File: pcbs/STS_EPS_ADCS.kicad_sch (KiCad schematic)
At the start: 22 parts, among them U10 MAX11632EEGT, U5 MAX11632EEGT, U6 MAX11632EEGT, U7 MAX11632EEGT, U8 MAX11632EEGT, U9 MAX11632EEGT

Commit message: Worked on STS1_EPS_1 and STS1_EPS_2.
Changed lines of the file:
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@@
-    (effects (font (size 1.27 1.27)) (justify right bottom))
-  )
-  (label "BATT_I" (at 48.26 129.54 180)
     (effects (font (size 1.27 1.27)) (justify right bottom))
   )
@@
     (effects (font (size 1.27 1.27)) (justify right bottom))
   )
-  (label "CENTER" (at 48.26 127 180)
-    (effects (font (size 1.27 1.27)) (justify right bottom))
-  )
   (label "Panel_Y-_5" (at 48.26 137.16 180)
     (effects (font (size 1.27 1.27)) (justify right bottom))
@@
     (effects (font (size 1.27 1.27)) (justify left bottom))
   )
-  (label "BATT_TEMP" (at 48.26 132.08 180)
-    (effects (font (size 1.27 1.27)) (justify right bottom))
-  )
   (label "Panel_Z-_5" (at 111.76 57.15 180)
     (effects (font (size 1.27 1.27)) (justify right bottom))
@@
     (effects (font (size 1.27 1.27)) (justify right))
   )
+  (hierarchical_label "CENTER" (shape input) (at 48.26 127 180)
+    (effects (font (size 1.27 1.27)) (justify right))
+  )
   (hierarchical_label "COBC_SPI_[1..6]" (shape input) (at 29.21 19.05 180)
     (effects (font (size 1.27 1.27)) (justify right))
@@
     (effects (font (size 1.27 1.27)) (justify right))
   )
+  (hierarchical_label "BATT_TEMP" (shape input) (at 48.26 132.08 180)
+    (effects (font (size 1.27 1.27)) (justify right))
+  )
+  (hierarchical_label "BATT_I" (shape input) (at 48.26 129.54 180)
+    (effects (font (size 1.27 1.27)) (justify right))
+  )

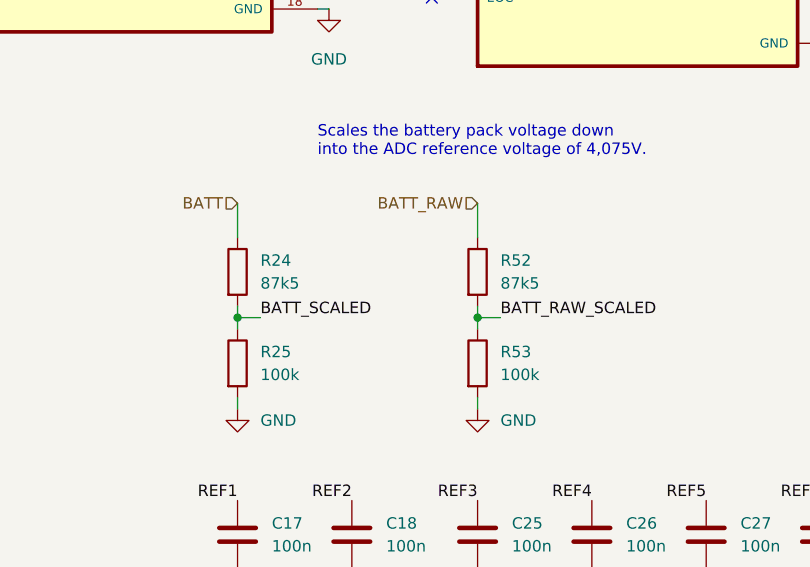
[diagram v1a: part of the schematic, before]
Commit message: Added part numbers to CSBI and inter EPS connectors. Also added some missing 3d files.
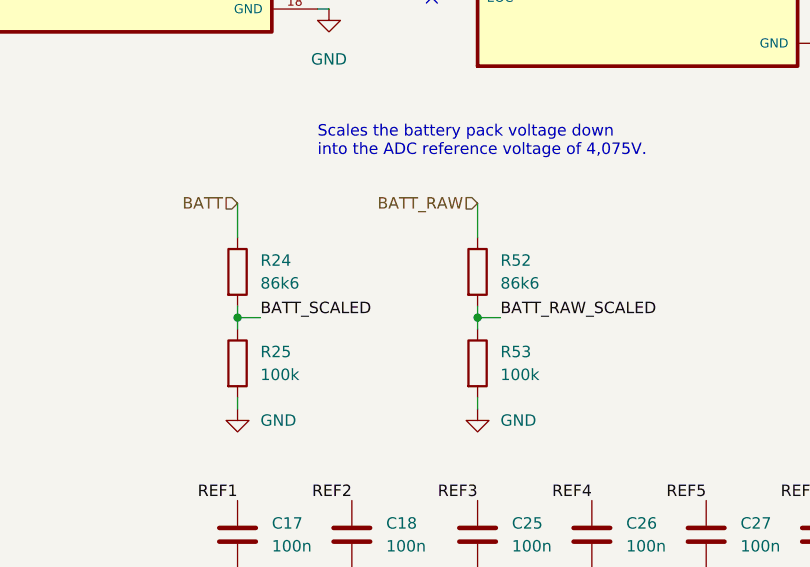
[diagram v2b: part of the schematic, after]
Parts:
- R24, R52: value 87k5 -> 86k6
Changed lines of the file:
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@@
       (effects (font (size 1.27 1.27)) (justify left))
     )
-    (property "Value" "87k5" (id 1) (at 210.82 125.7299 0)
+    (property "Value" "86k6" (id 1) (at 210.82 125.7299 0)
       (effects (font (size 1.27 1.27)) (justify left))
     )
@@
       (effects (font (size 1.27 1.27)) (justify left))
     )
-    (property "Value" "87k5" (id 1) (at 237.49 125.7299 0)
-      (effects (font (size 1.27 1.27)) (justify left))
-    )
+    (property "Value" "86k6" (id 1) (at 237.49 125.7299 0)
+      (effects (font (size 1.27 1.27)) (justify left))
+    )

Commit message: Fixed some warnings and errors.
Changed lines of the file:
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@@
 		)
 		(property "Value" "GND"
-			(at 210.82 140.9699 0)
+			(at 208.28 144.78 0)
 			(effects
 				(font
 					(size 1.27 1.27)
 				)
-				(justify left)
 			)
 		)
@@
 			)
 		)
-		(property "Description" ""
+		(property "Description" "Power symbol creates a global label with name \"GND\" , ground"
 			(at 208.28 139.7 0)
 			(effects
@@
 			)
 		)
-		(property "Description" ""
+		(property "Description" "Power symbol creates a global label with name \"GND\" , ground"
 			(at 247.65 157.48 0)
 			(effects
@@
 			)
 		)
-		(property "Description" ""
+		(property "Description" "Power symbol creates a global label with name \"GND\" , ground"
 			(at 109.22 158.75 0)
 			(effects
@@
 			)
 		)
-		(property "Description" ""
+		(property "Description" "Power symbol creates a global label with name \"GND\" , ground"
 			(at 283.21 30.48 0)
 			(effects
@@
 			)
 		)
-		(property "Description" ""
+		(property "Description" "Power symbol creates a global label with name \"GND\" , ground"
 			(at 96.52 182.88 0)
 			(effects
@@
 			)
 		)
-		(property "Description" ""
+		(property "Description" "Power symbol creates a global label with name \"GND\" , ground"
 			(at 160.02 186.69 0)
 			(effects
@@
 			)
 		)
-		(property "Description" ""
+		(property "Description" "Power symbol creates a global label with name \"GND\" , ground"
 			(at 166.37 26.67 0)
 			(effects
@@
 			)
 		)
-		(property "Description" ""
+		(property "Description" "Power symbol creates a global label with name \"GND\" , ground"
 			(at 273.05 157.48 0)
 			(effects
@@
 			)
 		)
-		(property "Description" ""
+		(property "Description" "Power symbol creates a global label with name \"GND\" , ground"
 			(at 171.45 34.29 0)
 			(effects
@@
 		)
 		(property "Value" "GND"
-			(at 237.49 140.9699 0)
+			(at 234.95 144.78 0)
 			(effects
 				(font
 					(size 1.27 1.27)
 				)
-				(justify left)
 			)
 		)
@@
 			)
 		)
-		(property "Description" ""
+		(property "Description" "Power symbol creates a global label with name \"GND\" , ground"
 			(at 234.95 139.7 0)
 			(effects
@@
 			)
 		)
-		(property "Description" ""
+		(property "Description" "Power symbol creates a global label with name \"GND\" , ground"
 			(at 226.06 26.67 0)
 			(effects
@@
 			)
 		)
-		(property "Description" ""
+		(property "Description" "Power symbol creates a global label with name \"GND\" , ground"
 			(at 96.52 95.25 0)
 			(effects
@@
 			)
 		)
-		(property "Description" ""
+		(property "Description" "Power symbol creates a global label with name \"GND\" , ground"
 			(at 260.35 157.48 0)
 			(effects
@@
 			)
 		)
-		(property "Description" ""
+		(property "Description" "Power symbol creates a global label with name \"GND\" , ground"
 			(at 220.98 157.48 0)
 			(effects
@@
 			)
 		)
-		(property "Description" ""
+		(property "Description" "Power symbol creates a global label with name \"GND\" , ground"
 			(at 208.28 157.48 0)
 			(effects
@@
 			)
 		)
-		(property "Description" ""
+		(property "Description" "Power symbol creates a global label with name \"GND\" , ground"
 			(at 111.76 125.73 0)
 			(effects
@@
 			)
 		)
-		(property "Description" ""
+		(property "Description" "Power symbol creates a global label with name \"GND\" , ground"
 			(at 170.18 67.31 0)
 			(effects
@@
 			)
 		)
-		(property "Description" ""
+		(property "Description" "Power symbol creates a global label with name \"GND\" , ground"
 			(at 48.26 154.94 0)
 			(effects
@@
 			)
 		)
-		(property "Description" ""
+		(property "Description" "Power symbol creates a global label with name \"GND\" , ground"
 			(at 279.4 99.06 0)
 			(effects
@@
 			)
 		)
-		(property "Description" ""
+		(property "Description" "Power symbol creates a global label with name \"GND\" , ground"
 			(at 166.37 118.11 0)
 			(effects
@@
 			)
 		)
-		(property "Description" ""
+		(property "Description" "Power symbol creates a global label with name \"GND\" , ground"
 			(at 102.87 114.3 0)
 			(effects
@@
 			)
 		)
-		(property "Description" ""
+		(property "Description" "Power symbol creates a global label with name \"GND\" , ground"
 			(at 160.02 95.25 0)
 			(effects
@@
 			)
 		)
-		(property "Description" ""
+		(property "Description" "Power symbol creates a global label with name \"GND\" , ground"
 			(at 101.6 26.67 0)
 			(effects
@@
 		)
 		(property "Value" "GND"
-			(at 218.44 100.838 0)
+			(at 218.44 100.33 0)
 			(effects
 				(font
@@
 			)
 		)
-		(property "Description" ""
+		(property "Description" "Power symbol creates a global label with name \"GND\" , ground"
 			(at 218.44 95.25 0)
 			(effects
@@
 			)
 		)
-		(property "Description" ""
+		(property "Description" "Power symbol creates a global label with name \"GND\" , ground"
 			(at 111.76 67.31 0)
 			(effects
@@
 			)
 		)
-		(property "Description" ""
+		(property "Description" "Power symbol creates a global label with name \"GND\" , ground"
 			(at 234.95 157.48 0)
 			(effects

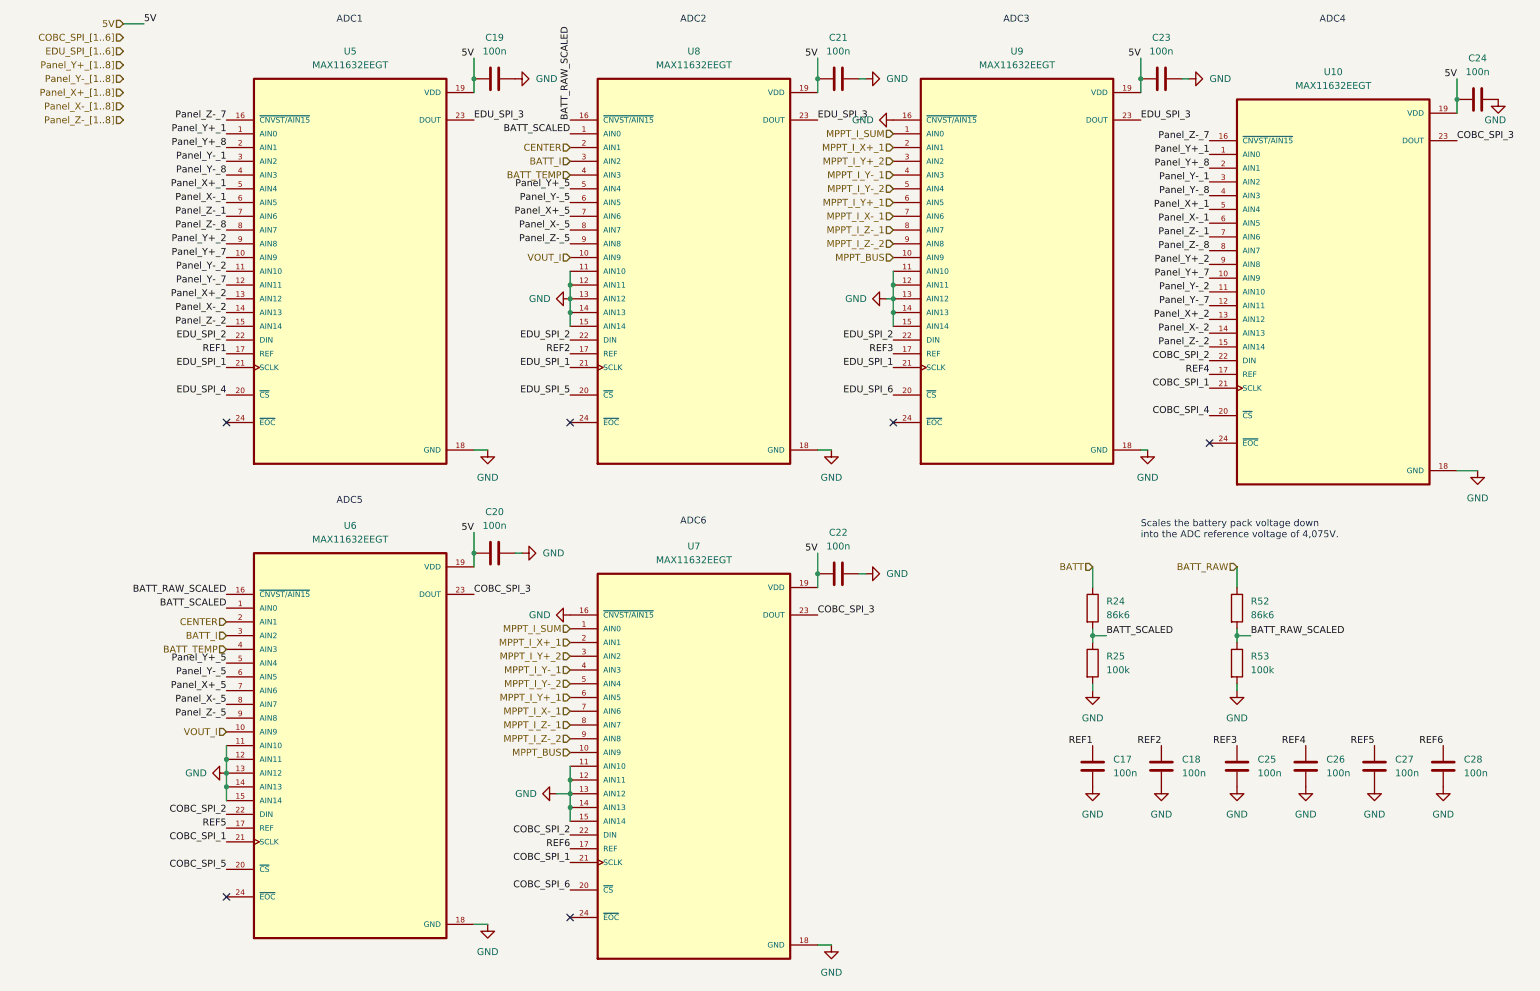
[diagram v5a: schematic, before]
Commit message: Fixed warnings and errors.
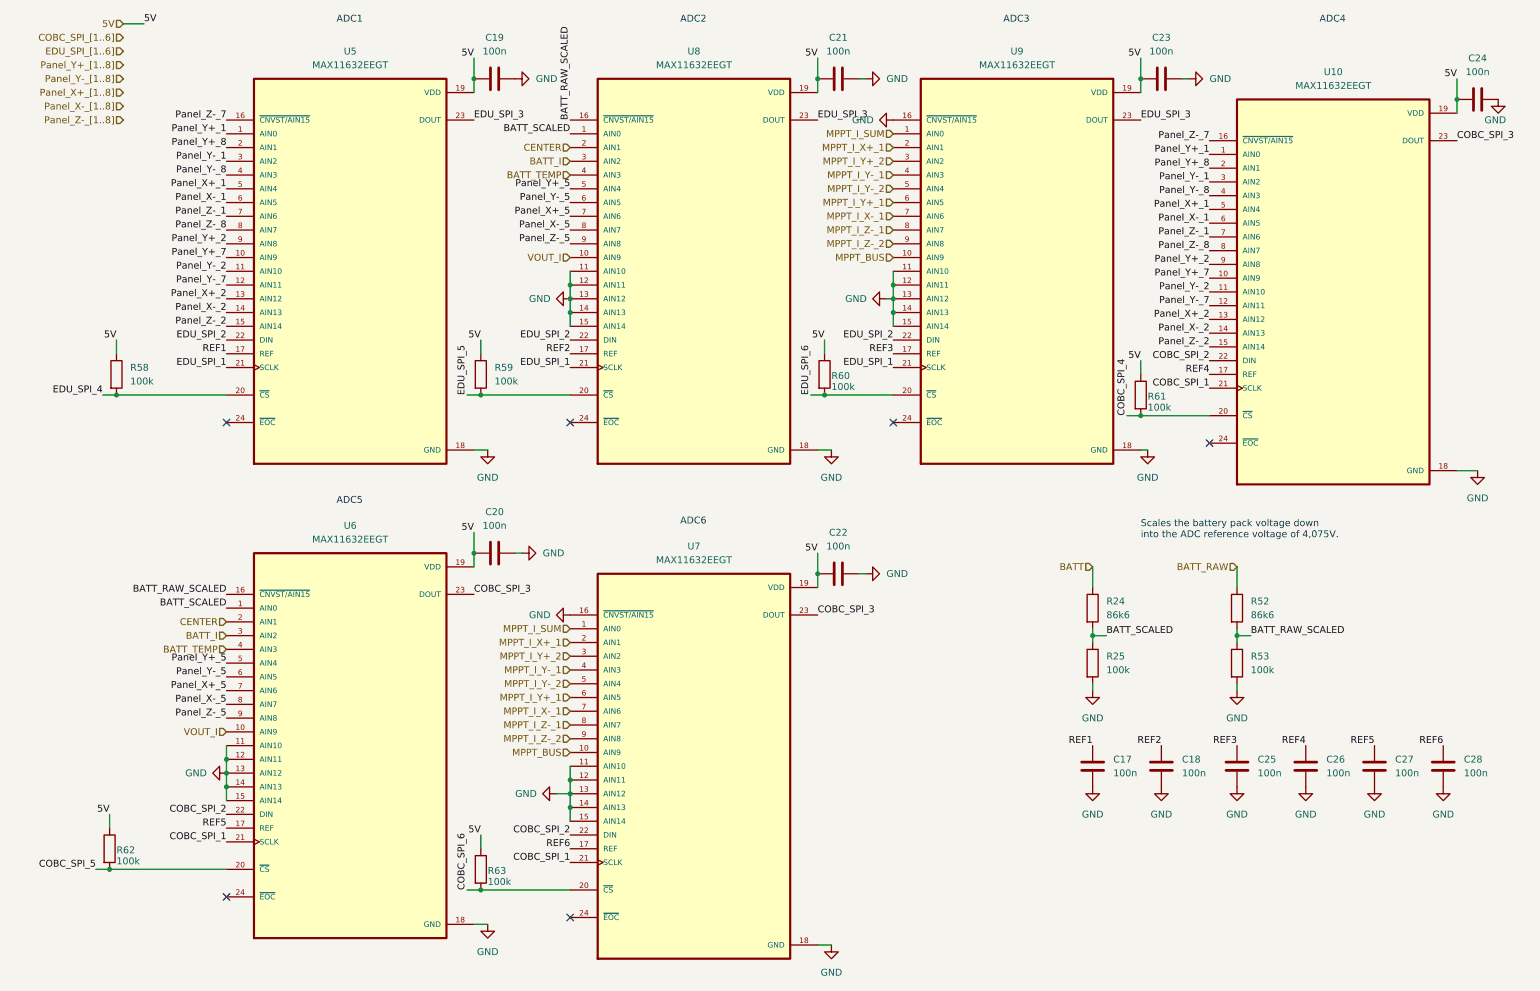
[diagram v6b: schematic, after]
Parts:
- added R58, R59, R60, R61, R62, R63: 100k, Resistor_SMD:R_0805_2012Metric, symbol Device:R
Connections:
- net 5V: now also R58.1, R59.1, R60.1, R61.1, R62.1, R63.1
- net COBC_SPI_4: now also R61.2
- net COBC_SPI_5: now also R62.2
- net COBC_SPI_6: now also R63.2
- net EDU_SPI_4: now also R58.2
- net EDU_SPI_5: now also R59.2
- net EDU_SPI_6: now also R60.2

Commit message: Intermediate commit.
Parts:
- removed R58, R59, R60: 100k, Resistor_SMD:R_0805_2012Metric, symbol Device:R

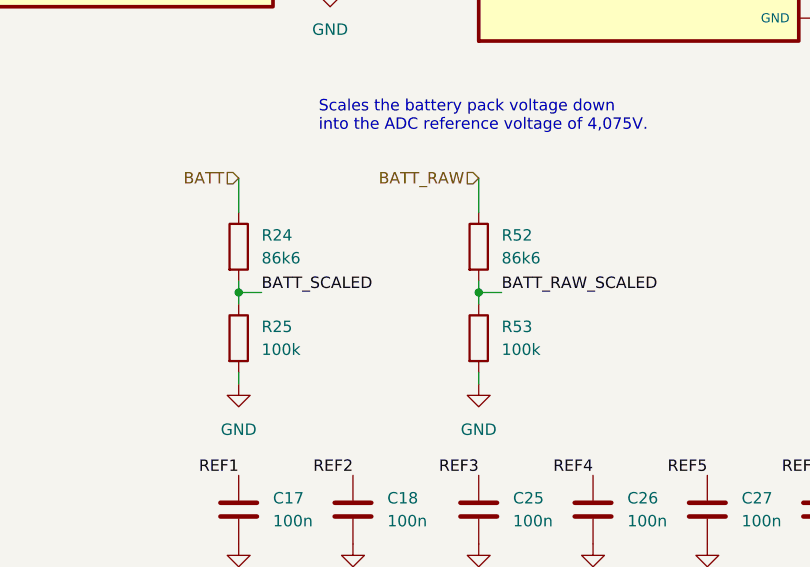
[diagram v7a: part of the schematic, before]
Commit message: Added tolerances to some resistors that should be precise.
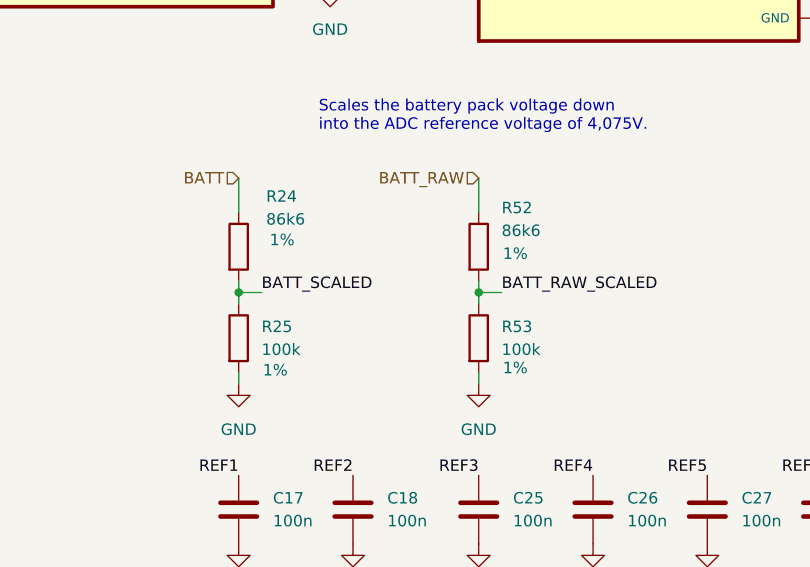
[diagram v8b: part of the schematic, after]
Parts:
- R24, R25, R52, R53: Tolerance (none) -> 1%
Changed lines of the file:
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@@
 		(on_board yes)
 		(dnp no)
-		(fields_autoplaced yes)
 		(property "Reference" "R24"
-			(at 210.82 123.1899 0)
+			(at 211.328 118.872 0)
 			(effects
 				(font
@@
 		)
 		(property "Value" "86k6"
-			(at 210.82 125.7299 0)
+			(at 211.328 121.412 0)
 			(effects
 				(font
@@
 				)
 				(hide yes)
+			)
+		)
+		(property "Tolerance" "1%"
+			(at 213.106 123.698 0)
+			(effects
+				(font
+					(size 1.27 1.27)
+				)
 			)
 		)
@@
 		(on_board yes)
 		(dnp no)
-		(fields_autoplaced yes)
 		(property "Reference" "R53"
 			(at 237.49 133.3499 0)
@@
 				)
 				(hide yes)
+			)
+		)
+		(property "Tolerance" "1%"
+			(at 239.014 137.922 0)
+			(effects
+				(font
+					(size 1.27 1.27)
+				)
 			)
 		)
@@
 		(on_board yes)
 		(dnp no)
-		(fields_autoplaced yes)
 		(property "Reference" "R25"
 			(at 210.82 133.3499 0)
@@
 				)
 				(hide yes)
+			)
+		)
+		(property "Tolerance" "1%"
+			(at 212.344 138.176 0)
+			(effects
+				(font
+					(size 1.27 1.27)
+				)
 			)
 		)
@@
 		(on_board yes)
 		(dnp no)
-		(fields_autoplaced yes)
 		(property "Reference" "R52"
-			(at 237.49 123.1899 0)
+			(at 237.49 120.142 0)
 			(effects
 				(font
@@
 		)
 		(property "Value" "86k6"
-			(at 237.49 125.7299 0)
+			(at 237.49 122.682 0)
 			(effects
 				(font
@@
 			)
 		)
+		(property "Tolerance" "1%"
+			(at 239.014 125.222 0)
+			(effects
+				(font
+					(size 1.27 1.27)
+				)
+			)
+		)
